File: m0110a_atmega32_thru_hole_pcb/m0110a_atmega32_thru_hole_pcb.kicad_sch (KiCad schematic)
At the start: 9 parts, among them J1 Conn_01x40_Pin, J2 ISP, J3 Serial, U2 ATmega32A-M, Y1 ATS08A-E - 8MHz

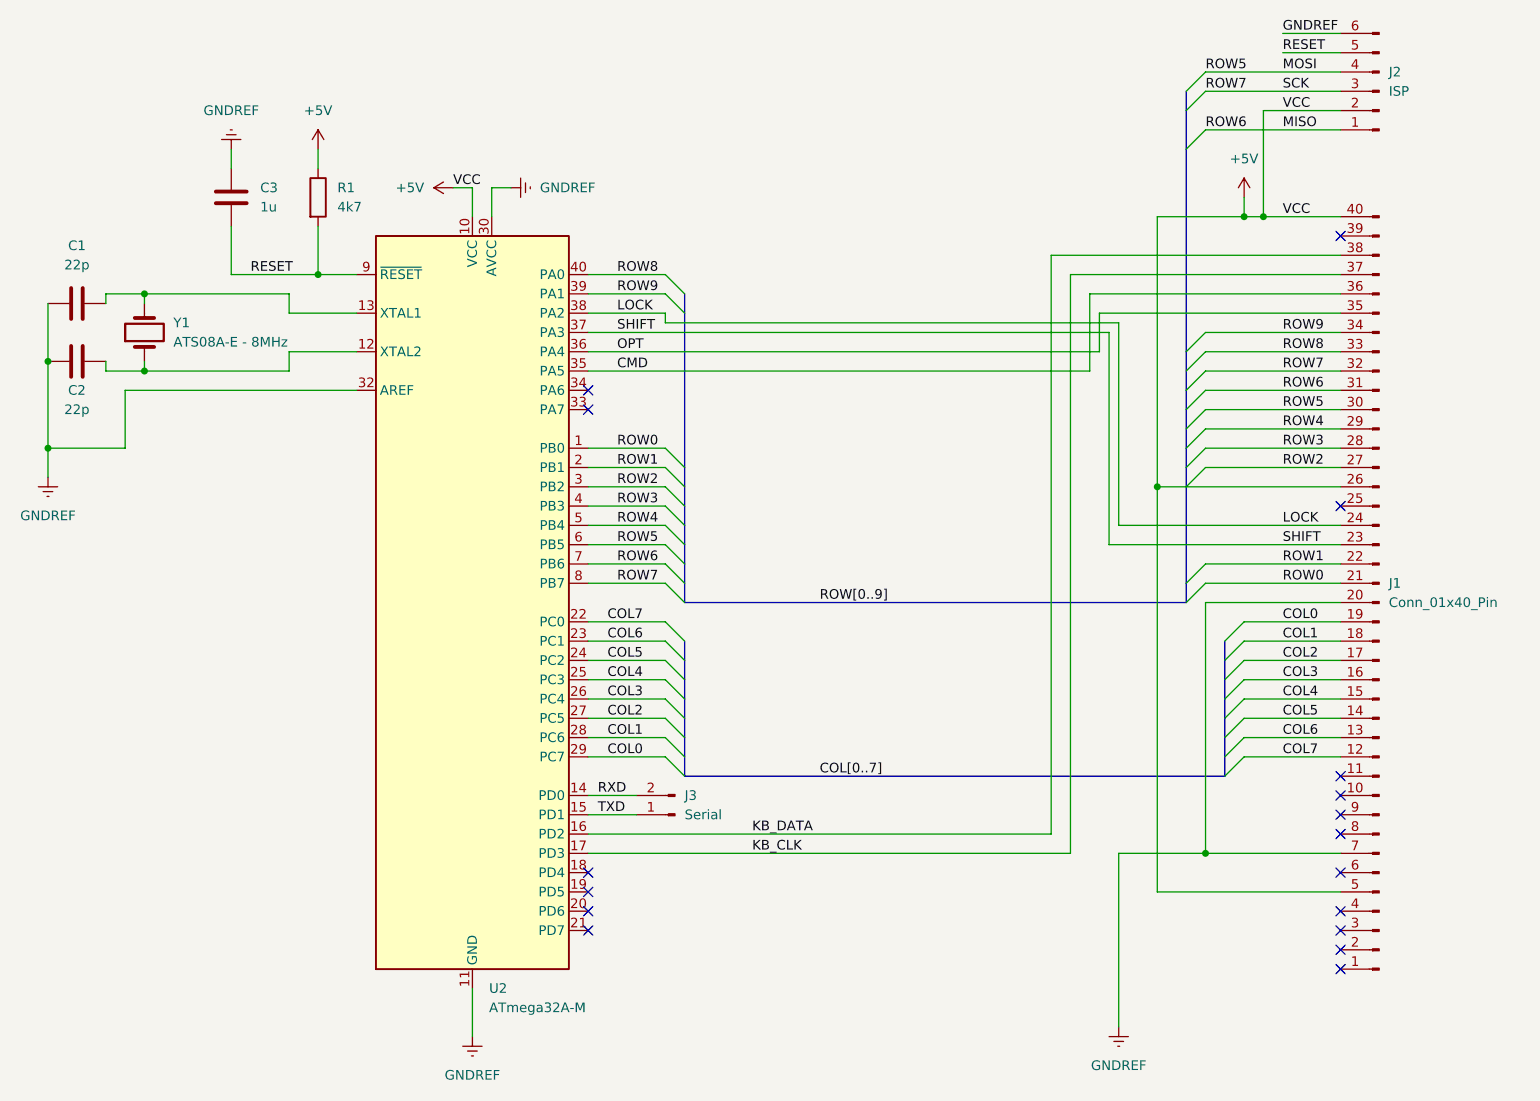
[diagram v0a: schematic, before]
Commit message: Switched from external to internal clocking
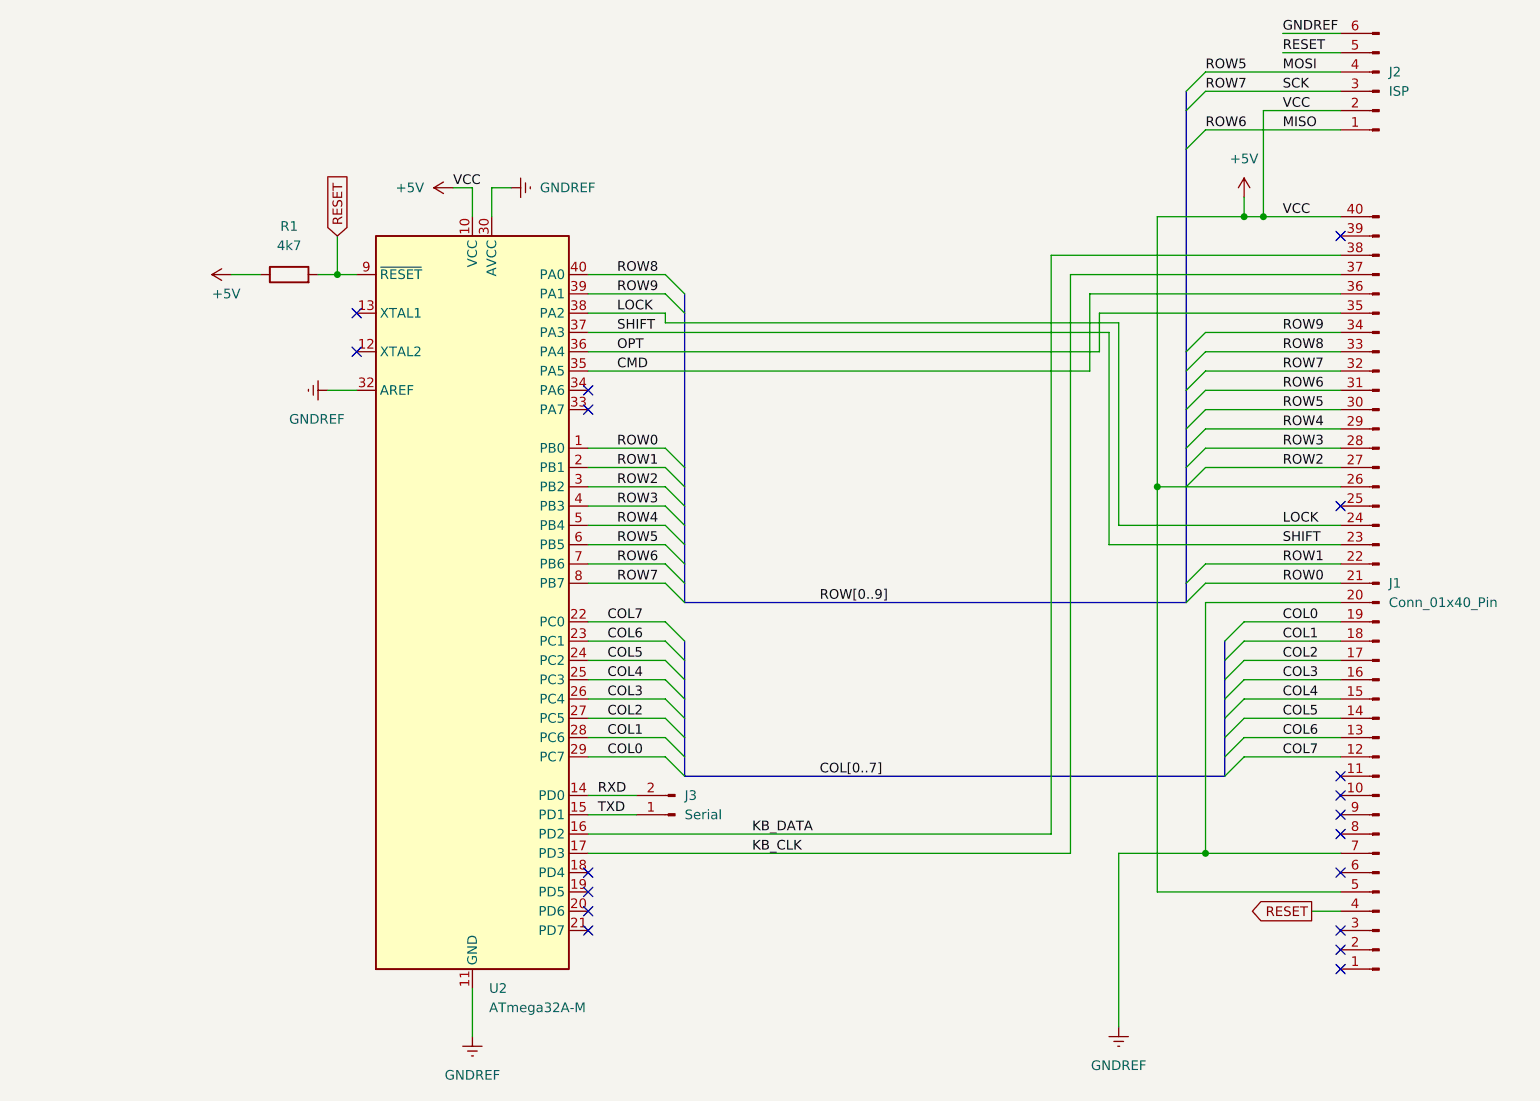
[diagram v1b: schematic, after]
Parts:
- removed C1, C2: 22p, Capacitor_THT:C_Disc_D3.4mm_W2.1mm_P2.50mm, symbol Device:C
- removed C3: 1u, Capacitor_THT:C_Rect_L7.0mm_W4.5mm_P5.00mm, symbol Device:C
- removed Y1: ATS08A-E - 8MHz, Crystal:Crystal_HC49-U_Vertical, symbol Device:Crystal
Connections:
- net RESET: now also J1.4 (Pin_4)
- no-connect marks 17 -> 18
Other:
- moved on the sheet: R1

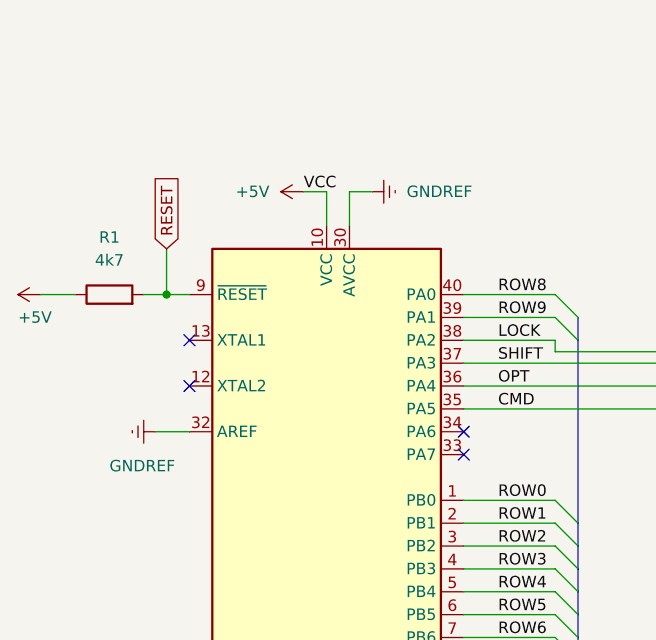
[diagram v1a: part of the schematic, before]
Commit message: Removed unneeded resistor and ground connections
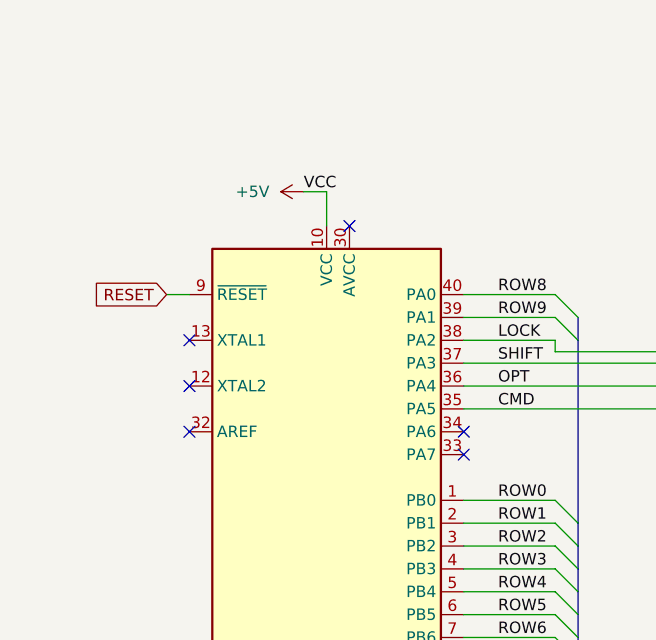
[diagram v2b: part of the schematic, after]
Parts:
- removed R1: 4k7, Resistor_THT:R_Axial_DIN0207_L6.3mm_D2.5mm_P7.62mm_Horizontal, symbol Device:R
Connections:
- net GNDREF: no longer U2.30 (AVCC), U2.32 (AREF)
- no-connect marks 18 -> 20
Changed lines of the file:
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@@
 (kicad_sch (version 20230121) (generator eeschema)
-  (paper "A")
+  (paper "USLetter")
   (junction (at 204.47 45.72) (diameter 0) (color 0 0 0 0)
   )
@@
   )
   (junction (at 193.04 81.28) (diameter 0) (color 0 0 0 0)
-  )
-  (junction (at 85.09 53.34) (diameter 0) (color 0 0 0 0)
   )
   (junction (at 199.39 129.54) (diameter 0) (color 0 0 0 0)
@@
   (no_connect (at 87.63 63.5))
   (no_connect (at 217.17 83.82))
+  (no_connect (at 105.41 45.72))
   (no_connect (at 217.17 142.24))
   (no_connect (at 217.17 132.08))
@@
   (no_connect (at 217.17 119.38))
   (no_connect (at 217.17 139.7))
+  (no_connect (at 87.63 68.58))
   (no_connect (at 118.11 134.62))
   (no_connect (at 217.17 48.26))
@@
     (stroke (width 0) (type default))
   )
-  (wire (pts (xy 105.41 41.91) (xy 105.41 45.72))
-    (stroke (width 0) (type default))
-  )
   (wire (pts (xy 199.39 68.58) (xy 217.17 68.58))
     (stroke (width 0) (type default))
@@
     (stroke (width 0) (type default))
   )
-  (wire (pts (xy 71.12 53.34) (xy 74.93 53.34))
-    (stroke (width 0) (type default))
-  )
   (bus (pts (xy 201.93 111.76) (xy 201.93 114.3))
     (stroke (width 0) (type default))
@@
     (stroke (width 0) (type default))
   )
-  (wire (pts (xy 85.09 53.34) (xy 82.55 53.34))
-    (stroke (width 0) (type default))
-  )
   (bus (pts (xy 130.81 91.44) (xy 130.81 93.98))
     (stroke (width 0) (type default))
@@
     (stroke (width 0) (type default))
   )
-  (wire (pts (xy 85.09 48.26) (xy 85.09 53.34))
-    (stroke (width 0) (type default))
-  )
   (bus (pts (xy 201.93 114.3) (xy 201.93 116.84))
     (stroke (width 0) (type default))
@@
     (stroke (width 0) (type default))
   )
-  (wire (pts (xy 83.82 68.58) (xy 87.63 68.58))
-    (stroke (width 0) (type default))
-  )
   (bus (pts (xy 130.81 93.98) (xy 130.81 96.52))
     (stroke (width 0) (type default))
@@
     (stroke (width 0) (type default))
   )
-  (wire (pts (xy 107.95 41.91) (xy 105.41 41.91))
-    (stroke (width 0) (type default))
-  )
   (wire (pts (xy 204.47 114.3) (xy 217.17 114.3))
     (stroke (width 0) (type default))
@@
     (effects (font (size 1.27 1.27)) (justify left bottom))
   )
-  (global_label "RESET" (shape input) (at 85.09 48.26 90) (fields_autoplaced)
-    (effects (font (size 1.27 1.27)) (justify left))
-    (property "Intersheetrefs" "${INTERSHEET_REFS}" (at 85.09 39.5297 90)
-      (effects (font (size 1.27 1.27)) (justify left) hide)
+  (global_label "RESET" (shape input) (at 85.09 53.34 180) (fields_autoplaced)
+    (effects (font (size 1.27 1.27)) (justify right))
+    (property "Intersheetrefs" "${INTERSHEET_REFS}" (at 76.3597 53.34 0)
+      (effects (font (size 1.27 1.27)) (justify right) hide)
     )
   )
@@
     )
   )
-  (symbol (lib_id "power:+5V") (at 71.12 53.34 90) (unit 1)
-    (in_bom yes) (on_board yes) (dnp no)
-    (property "Reference" "#PWR04" (at 74.93 53.34 0)
-      (effects (font (size 1.27 1.27)) hide)
-    )
-    (property "Value" "+5V" (at 68.58 55.88 90)
-      (effects (font (size 1.27 1.27)) (justify right))
-    )
-    (property "Footprint" "" (at 71.12 53.34 0)
-      (effects (font (size 1.27 1.27)) hide)
-    )
-    (property "Datasheet" "" (at 71.12 53.34 0)
-      (effects (font (size 1.27 1.27)) hide)
-    )
-    (pin "1")
-    (instances
-      (project "m0110a_atmega32_thru_hole_pcb"
-        (path "/a1198300-da90-46e8-a8a2-d3cc0b3c7a24"
-          (reference "#PWR04") (unit 1)
-        )
-      )
-    )
-  )
   (symbol (lib_id "power:+5V") (at 204.47 43.18 0) (unit 1)
     (in_bom yes) (on_board yes) (dnp no) (fields_autoplaced)
@@
     )
   )
-  (symbol (lib_id "power:GNDREF") (at 83.82 68.58 270) (unit 1)
-    (in_bom yes) (on_board yes) (dnp no)
-    (property "Reference" "#PWR01" (at 77.47 68.58 0)
-      (effects (font (size 1.27 1.27)) hide)
-    )
-    (property "Value" "GNDREF" (at 78.74 72.39 90)
-      (effects (font (size 1.27 1.27)) (justify left))
-    )
-    (property "Footprint" "" (at 83.82 68.58 0)
-      (effects (font (size 1.27 1.27)) hide)
-    )
-    (property "Datasheet" "" (at 83.82 68.58 0)
-      (effects (font (size 1.27 1.27)) hide)
-    )
-    (pin "1")
-    (instances
-      (project "m0110a_atmega32_thru_hole_pcb"
-        (path "/a1198300-da90-46e8-a8a2-d3cc0b3c7a24"
-          (reference "#PWR01") (unit 1)
-        )
-      )
-    )
-  )
-  (symbol (lib_id "power:GNDREF") (at 107.95 41.91 90) (unit 1)
-    (in_bom yes) (on_board yes) (dnp no) (fields_autoplaced)
-    (property "Reference" "#PWR02" (at 114.3 41.91 0)
-      (effects (font (size 1.27 1.27)) hide)
-    )
-    (property "Value" "GNDREF" (at 111.76 41.91 90)
-      (effects (font (size 1.27 1.27)) (justify right))
-    )
-    (property "Footprint" "" (at 107.95 41.91 0)
-      (effects (font (size 1.27 1.27)) hide)
-    )
-    (property "Datasheet" "" (at 107.95 41.91 0)
-      (effects (font (size 1.27 1.27)) hide)
-    )
-    (pin "1")
-    (instances
-      (project "m0110a_atmega32_thru_hole_pcb"
-        (path "/a1198300-da90-46e8-a8a2-d3cc0b3c7a24"
-          (reference "#PWR02") (unit 1)
-        )
-      )
-    )
-  )
   (symbol (lib_id "power:GNDREF") (at 187.96 152.4 0) (unit 1)
     (in_bom yes) (on_board yes) (dnp no) (fields_autoplaced)
@@
         )
       )
-    )
-  )
-  (symbol (lib_id "Device:R") (at 78.74 53.34 90) (unit 1)
-    (in_bom yes) (on_board yes) (dnp no) (fields_autoplaced)
-    (property "Reference" "R1" (at 78.74 46.99 90)
-      (effects (font (size 1.27 1.27)))
-    )
-    (property "Value" "4k7" (at 78.74 49.53 90)
-      (effects (font (size 1.27 1.27)))
-    )
-    (property "Footprint" "Resistor_THT:R_Axial_DIN0207_L6.3mm_D2.5mm_P7.62mm_Horizontal" (at 78.74 55.118 90)
-      (effects (font (size 1.27 1.27)) hide)
-    )
-    (property "Datasheet" "~" (at 78.74 53.34 0)
-      (effects (font (size 1.27 1.27)) hide)
-    )
-    (pin "1")
-    (pin "2")
-    (instances
-      (project "m0110a_atmega32_thru_hole_pcb"
-        (path "/a1198300-da90-46e8-a8a2-d3cc0b3c7a24"
-          (reference "R1") (unit 1)
-        )
-      )

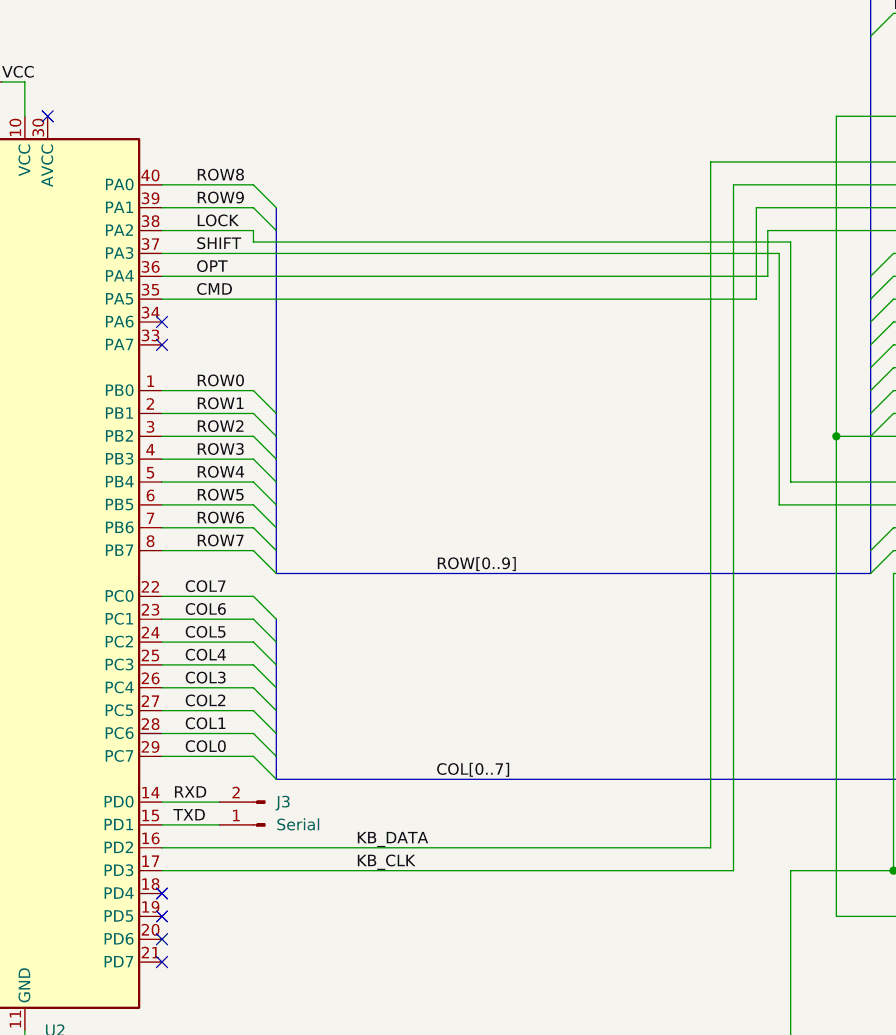
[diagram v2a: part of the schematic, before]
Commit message: Swapped data and clk for easier layout. V 2.1
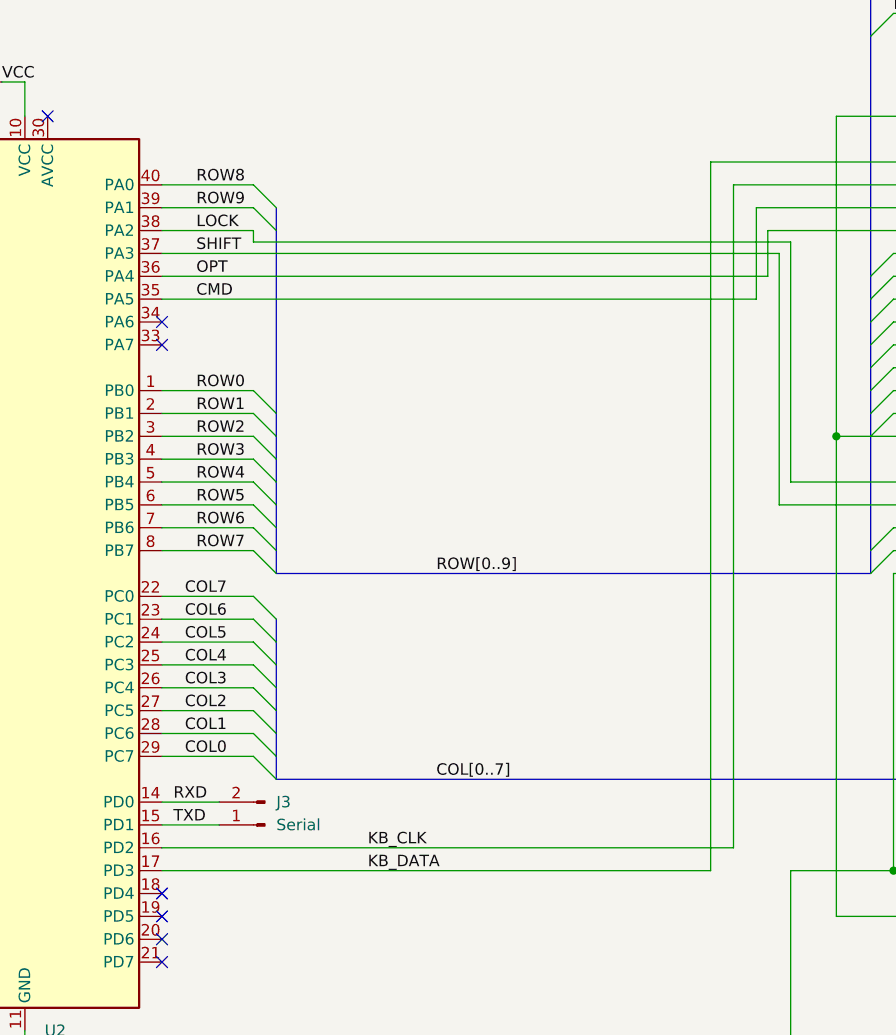
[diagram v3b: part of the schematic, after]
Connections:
- net KB_CLK: now also U2.16 (PD2); no longer U2.17 (PD3)
- net KB_DATA: now also U2.17 (PD3); no longer U2.16 (PD2)
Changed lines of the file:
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@@
-    (stroke (width 0) (type default))
-  )
-  (wire (pts (xy 118.11 129.54) (xy 181.61 129.54))
     (stroke (width 0) (type default))
   )
@@
     (stroke (width 0) (type default))
   )
+  (wire (pts (xy 179.07 50.8) (xy 179.07 129.54))
+    (stroke (width 0) (type default))
+  )
   (bus (pts (xy 196.85 81.28) (xy 196.85 93.98))
     (stroke (width 0) (type default))
@@
     (stroke (width 0) (type default))
   )
-  (wire (pts (xy 118.11 127) (xy 179.07 127))
-    (stroke (width 0) (type default))
-  )
   (wire (pts (xy 118.11 124.46) (xy 124.46 124.46))
     (stroke (width 0) (type default))
@@
     (stroke (width 0) (type default))
   )
+  (wire (pts (xy 118.11 127) (xy 181.61 127))
+    (stroke (width 0) (type default))
+  )
   (wire (pts (xy 118.11 91.44) (xy 128.27 91.44))
     (stroke (width 0) (type default))
@@
     (stroke (width 0) (type default))
   )
-  (wire (pts (xy 179.07 127) (xy 179.07 50.8))
-    (stroke (width 0) (type default))
-  )
   (wire (pts (xy 118.11 55.88) (xy 128.27 55.88))
     (stroke (width 0) (type default))
@@
     (stroke (width 0) (type default))
   )
+  (wire (pts (xy 118.11 129.54) (xy 179.07 129.54))
+    (stroke (width 0) (type default))
+  )
   (wire (pts (xy 199.39 129.54) (xy 217.17 129.54))
     (stroke (width 0) (type default))
@@
     (stroke (width 0) (type default))
   )
+  (wire (pts (xy 181.61 127) (xy 181.61 53.34))
+    (stroke (width 0) (type default))
+  )
   (wire (pts (xy 204.47 111.76) (xy 217.17 111.76))
     (stroke (width 0) (type default))
@@
     (stroke (width 0) (type default))
   )
-  (wire (pts (xy 181.61 129.54) (xy 181.61 53.34))
-    (stroke (width 0) (type default))
-  )
   (wire (pts (xy 193.04 81.28) (xy 193.04 45.72))
     (stroke (width 0) (type default))
@@
     (effects (font (size 1.27 1.27)) (justify left bottom))
   )
-  (label "KB_CLK" (at 139.7 129.54 0) (fields_autoplaced)
+  (label "KB_CLK" (at 140.97 127 0) (fields_autoplaced)
     (effects (font (size 1.27 1.27)) (justify left bottom))
   )
@@
     (effects (font (size 1.27 1.27)) (justify left bottom))
   )
-  (label "KB_DATA" (at 139.7 127 0) (fields_autoplaced)
-    (effects (font (size 1.27 1.27)) (justify left bottom))
-  )
+  (label "KB_DATA" (at 140.97 129.54 0) (fields_autoplaced)
+    (effects (font (size 1.27 1.27)) (justify left bottom))
+  )
